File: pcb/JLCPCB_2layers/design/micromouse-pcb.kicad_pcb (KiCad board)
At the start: 2 copper layers, 100 x 120 mm, 135 parts, among them J1 BATT_IN_2S, J10 BATT_IN_XT60 (parallel option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, J5 MOTOR_A_N20_ENCODER, J6 MOTOR_B_N20_ENCODER, J7 USB-C rear (GCT USB4105; VBUS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, Q1 Q_PMOS reverse guard (DMP3098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, Q16 BSS138 (real part; Q_NMOS_GSD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, Q17 BSS138 (real part; Q_NMOS_GSD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, Q18 BSS138 (real part; Q_NMOS_GSD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, Q2 PT334-6B (5mm filtered PT; LO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, Q28 BSS84 (PMOS indicator driver;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, Q29 BSS84 (PMOS indicator driver;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, Q3 PT334-6B (5mm filtered PT; LO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, Q30 BSS84 (PMOS indicator driver;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, Q31 BSS84 (PMOS indicator driver;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, Q32 BSS84 (PMOS indicator driver;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, Q33 BSS84 (PMOS indicator driver;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, Q34 MMBT2222A (buzzer low-side dr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, Q4 PT334-6B (5mm filtered PT; LO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, Q5 PT334-6B (5mm filtered PT; LO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, Q6 PT334-6B (5mm filtered PT; LO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, Q7 PT334-6B (5mm filtered PT; LO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, SW1 BTN_A (start / BOOT), SW2 RESET, SW3 BTN_B, SW4 BTN_C, SW5 PWR ALL (PCM12SMTR slide; sli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, SW6 PWR MOTORS (PCM12SMTR slide; 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, U1 AP63203WU-7 (fixed 3.3V 2A bu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, U2 TB6612FNG, U3 ESP32-S3-WROOM-1-N8R2 (quad P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, U6 USBLC6-2SC6 (SOT-23-6; 2P6 ba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, U7 TPS54302DDCR (6.0V/3A motor b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, U8 BNO055 (9-axis IMU + fusion; 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

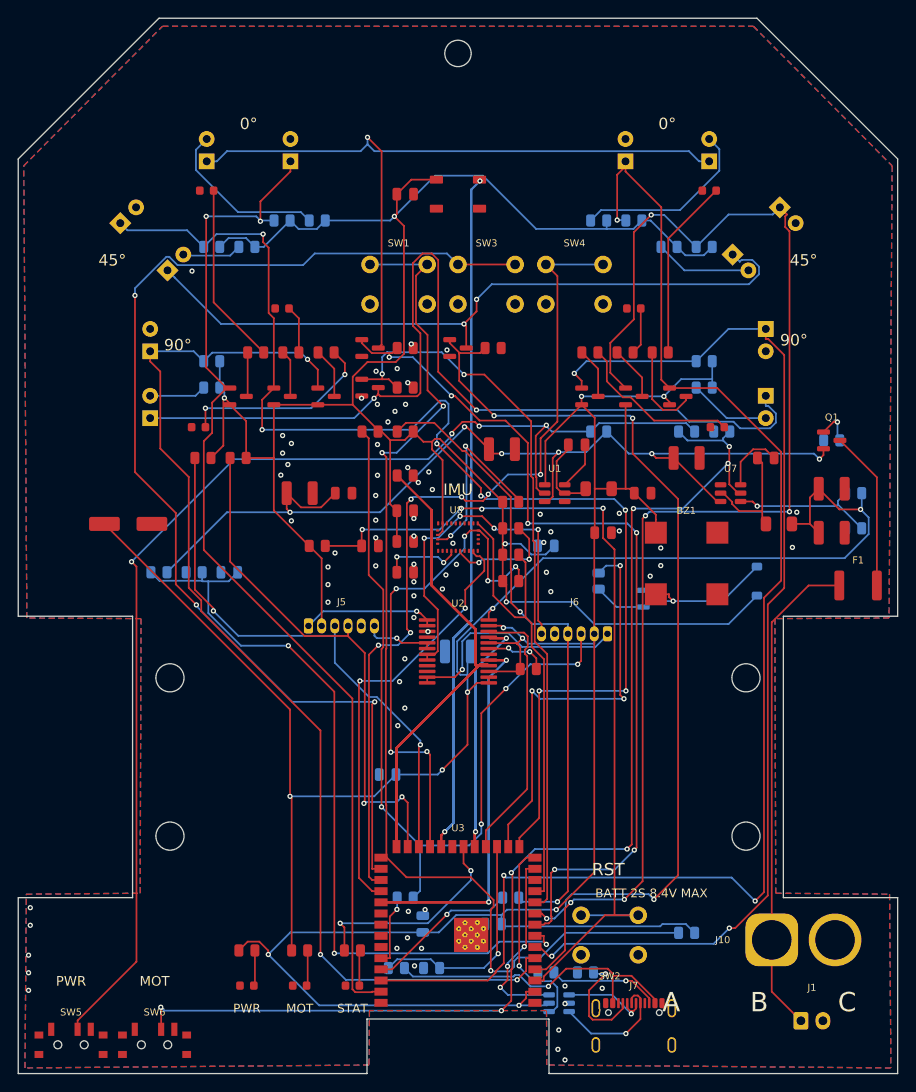
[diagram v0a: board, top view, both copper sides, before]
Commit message: 2-layer PRODUCTION: power-width re-route + full check battery + validated JLC package
Final electronics check (all gates PASS):
- NEW fw/sim_imu.py -- IMU accessibility proven per user request: all 28 BNO055
  pins verified against the official Bosch datasheet Table 5-1 (fetched + read),
  I2C bus electricals (4.7k pull-ups, 199ns rise @400kHz, no contention), and a
  behavioral register-level replay of imu_init()/imu_selftest() (addr 0x28 from
  the COM3 strap, CHIP_ID retry vs 400ms power-on, mode timing vs Table 3-6,
  CLK_SEL kept internal since XIN32/XOUT32 are NC, NDOF fusion up, heading +
  gyro reads). 44/44 PASS.
- AMPACITY FIX: Freerouting had routed every power rail at its 0.2mm default.
  Added tools/dsn_power_class.py (DSN class surgery: power 0.5mm, PLUS3V3
  0.4mm) + tools/route_pipeline.py (motor-bay open + hard-net pre-route +
  inset boundary + DSN export). Re-routed: BATT_RAW/VM_BATT/VM_6V/SW_6V all
  0.5mm, PLUS3V3 0.4mm -> IPC-2152 satisfied with margin. Score 994.73,
  0 signal unrouted.
- sim_flash netlist path fixed (design/ not pcb/); ALL STAGES PASS.
- check_pins 28/28, sim_preflight PASS, impedance PASS, ERC 0.
- DRC 0 errors / 0 parity; GND unconnected floor = 7 non-critical items
  (documented waiver in export_fab: redundant U8 GND pads 2/25 + pour slivers).

JLCPCB compliance + availability:
- Board vs JLC 2-layer limits: min track 0.2 (>=0.127), via 0.6/0.3, clearance
  rule 0.127 -- all within standard capability.
- LCSC map: 44/44 BOM MPNs mapped. BNO055 (C93216) re-verified 2026-07-21:
  LCSC retail down to 2 units -- RESERVE at checkout or pre-source (note
  updated in jlcpcb_lcsc_map.py).

Production package (design/fab_release/jlcpcb/, committed):
- gerbers zip (9 layers, 2-layer set -- export_fab fixed off the 4-layer
  In1/In2 list), Excellon drill with 3.2/3.0 NPTH mounts, BOM + CPL xlsx/csv,
  THT reference.
- NEW tools/validate_jlc_files.py: mechanical JLC-compatibility gate (RS-274X
  headers, aperture >= 0.127mm, outline s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
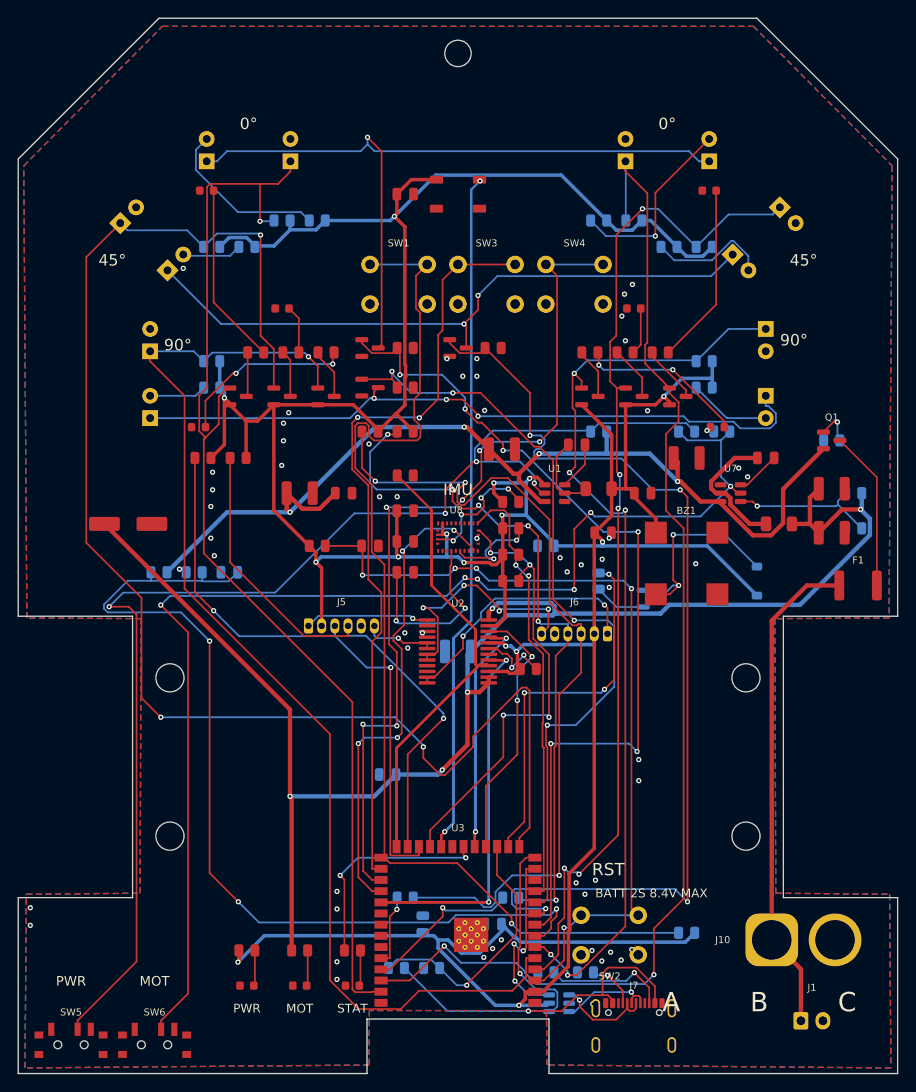
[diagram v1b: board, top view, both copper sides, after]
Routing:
- net BIN2: track 153.2 -> 99.1 mm
- net RGB_DATA: track 200.9 -> 153.2 mm
- net USER_BTN2: track 130.1 -> 87.2 mm, vias 3 -> 2
- net WALL4_SENSE: track 153.0 -> 115.3 mm
- net EMIT_SIDE_K: track 109.4 -> 79.0 mm, vias 2 -> 3
- net PLUS3V3: track 493.1 -> 465.8 mm, vias 11 -> 15
- net WALL3_SENSE: track 143.3 -> 165.8 mm, vias 7 -> 3
- net WALL2_SENSE: track 158.0 -> 139.7 mm, vias 3 -> 2
- net VBAT_SENSE: track 89.9 -> 106.2 mm
- net MOTB_N: track 42.1 -> 27.9 mm
- net WALL6_SENSE: track 121.9 -> 107.7 mm, vias 3 -> 5
- net Net-(U8-CAP): track 9.04 -> 21.5 mm
- net WALL_EMIT_DIAG: track 103.4 -> 114.7 mm
- net WALL1_SENSE: track 116.9 -> 126.6 mm, vias 2 -> 1
- net ESP_EN: track 102.9 -> 93.8 mm, vias 4 -> 5
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
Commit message: 2-layer BOM: stocked JLC parts for the LED + buzzer lines (user assembly review)
From the user's JLCPCB BOM-matching screenshots:

- Indicator LEDs (D23-D28, D30, D31, D33): the multi-line match warning is
  by-design (one red 0603 LED reused across all indicator roles), BUT the
  matched C5875723 has 0 in JLC's assembly pool (LCSC-retail-only). SUB to
  C2286 / KT-0603R -- JLC Basic tier, 3.59M stock (2026-07-21), 0603 pad- and
  Vf-compatible (1.8-2.4V), 300mcd; series resistors unchanged. Also fixed the
  stale "green"/"blue" Value labels at the schematic source: every indicator
  is physically RED (design reuses the wall-indicator part).
- Buzzer BZ1: C3811795 (JLC-consigned listing) hit Inventory shortage. The
  in-stock row is the SAME MPN (CUI CMT-8504-100-SMT-TR) under the regular
  LCSC listing C22359707 (104 stock) -- exact drop-in, verified not a
  substitute. BOM now carries C22359707.

Propagated: schematic + netlist regenerated, ERC 0, check_pins 28/28,
sim_imu PASS, sync_board_meta (2 values), DRC 0 errors / 0 parity,
export_fab ALL GATES, JLC package re-exported + validate_jlc_files ALL PASS.
Board copper untouched (diff = 2 value strings).

Co-Authored-By: Claude Fable 5 <noreply@anthropic.com>
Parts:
- D30: value Power LED 0603 green (JLC good-stock) -> Power LED 0603 red (JLC good-stock)
- D31: value Status LED 0603 blue (JLC good-stock) -> Status LED 0603 red (JLC good-stock)
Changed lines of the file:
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@@
 			)
 		)
-		(property "Value" "Status LED 0603 blue (JLC good-stock)"
+		(property "Value" "Status LED 0603 red (JLC good-stock)"
 			(at 0 1.43 0)
 			(layer "F.Fab")
@@
 			)
 		)
-		(property "Value" "Power LED 0603 green (JLC good-stock)"
+		(property "Value" "Power LED 0603 red (JLC good-stock)"
 			(at 0 1.43 0)
 			(layer "F.Fab")

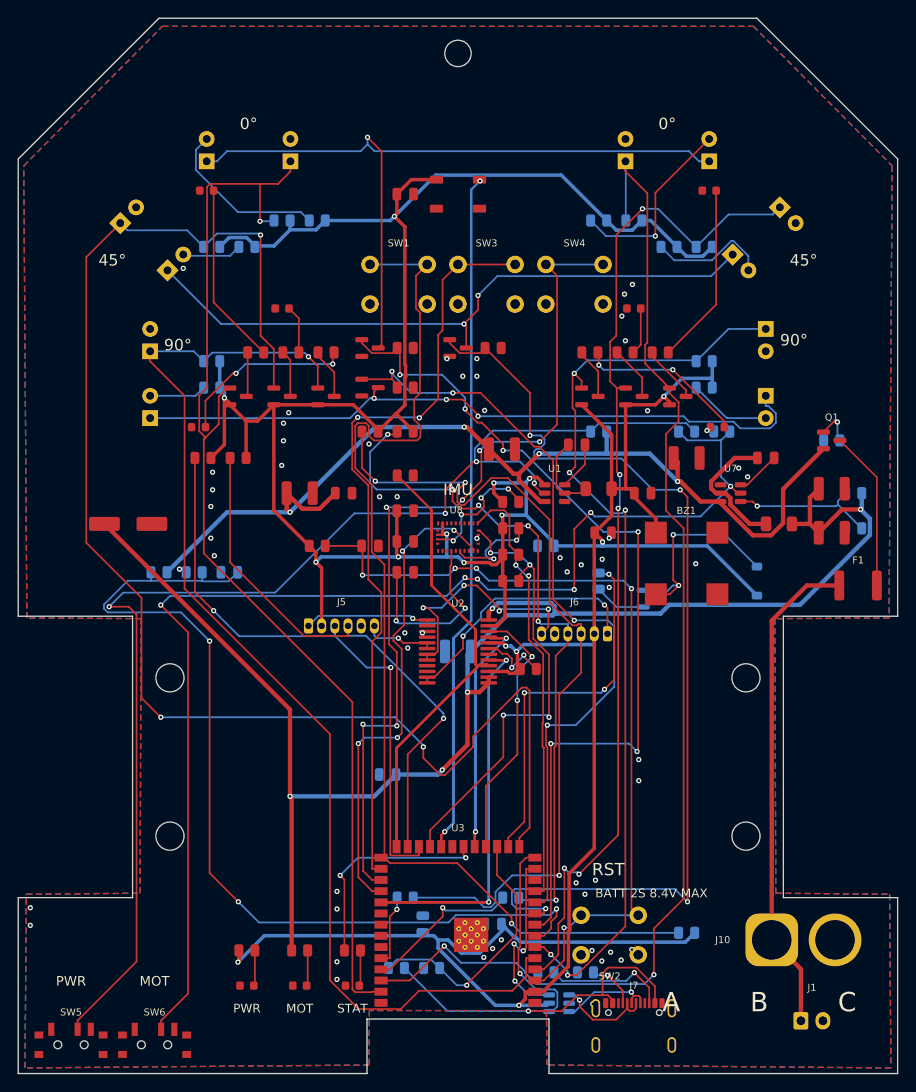
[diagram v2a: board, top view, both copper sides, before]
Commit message: 2-layer PRODUCTION: final JLCPCB + Lion Circuits release (wall sensors only)
Production-ready release for the 2-layer micromouse board (wall sensors
only, no line array/mux/JTAG): U8 (IMU) + U2 (motor driver) flipped to
the bottom layer, full clean-slate Freerouting re-route, GND pour
fragment bridging, BOM duplicate-part merge, and DRC cleanup (0 errors,
0 warnings). Includes matching production folders for both JLCPCB and
Lion Circuits (BOM, CPL, gerbers).

Co-Authored-By: Claude Sonnet 5 <noreply@anthropic.com>
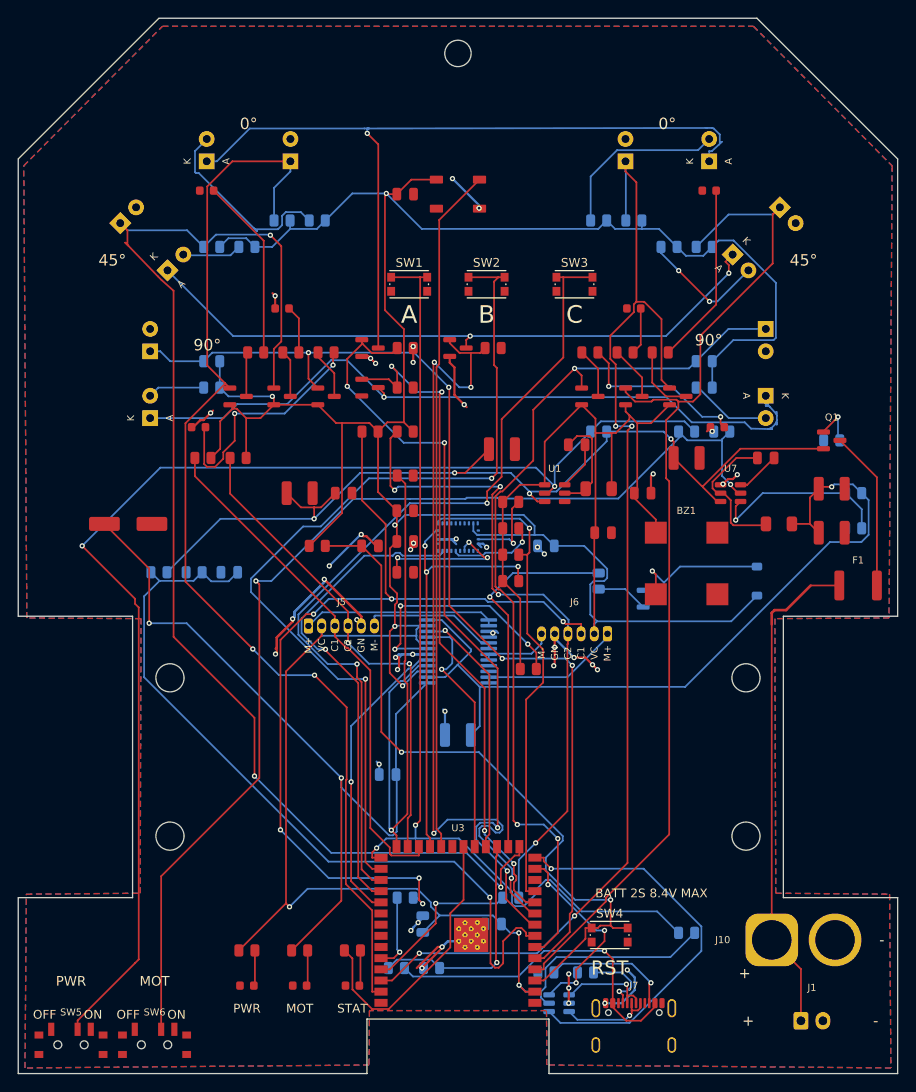
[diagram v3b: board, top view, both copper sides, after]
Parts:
- SW1: footprint Button_Switch_THT:SW_PUSH_6mm -> Button_Switch_SMD:SW_Push_1P1T_NO_CK_KMR2
- SW2: value RESET -> BTN_B; footprint Button_Switch_THT:SW_PUSH_6mm -> Button_Switch_SMD:SW_Push_1P1T_NO_CK_KMR2
- SW3: value BTN_B -> BTN_C; footprint Button_Switch_THT:SW_PUSH_6mm -> Button_Switch_SMD:SW_Push_1P1T_NO_CK_KMR2
- SW4: value BTN_C -> RESET; footprint Button_Switch_THT:SW_PUSH_6mm -> Button_Switch_SMD:SW_Push_1P1T_NO_CK_KMR2
- U2, U8: moved to B.Cu
- moved SW4 76.6 mm to (67.2, 104.2)
- moved SW2 72.6 mm to (53.2, 30.2)
- moved SW3 13.4 mm to (63.2, 30.2)
- moved C11 9.50 mm to (50.0, 81.5)
- moved SW1 4.99 mm to (44.5, 30.2)
- turned U2 to 180 degrees
- turned U8 to 180 degrees
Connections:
- SW2 pad 1: ESP_EN -> USER_BTN2
- SW3 pad 1: USER_BTN2 -> USER_BTN3
- SW4 pad 1: USER_BTN3 -> ESP_EN
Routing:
- net GND: track 0.00 -> 127.1 mm, vias 58 -> 45
- net RGB_DATA: track 153.2 -> 78.1 mm, vias 2 -> 0
- net BIN1: track 82.3 -> 33.8 mm, vias 2 -> 1
- net PLUS3V3: track 465.8 -> 508.3 mm, vias 15 -> 8
- net BIN2: track 99.1 -> 65.1 mm, vias 0 -> 1
- net USB_DP: track 22.5 -> 46.4 mm
- net WALL_EMIT_DIAG: track 114.7 -> 93.0 mm
- net AIN1: track 49.2 -> 28.9 mm, vias 2 -> 1
- net Net-(U2-STBY): track 8.30 -> 28.4 mm, vias 2 -> 3
- net WALL3_SENSE: track 165.8 -> 146.0 mm
- net MOTB_N: track 27.9 -> 8.27 mm, vias 4 -> 0
- net VBAT_SENSE: track 106.2 -> 89.6 mm, vias 3 -> 1
- net MOT_EN: track 140.5 -> 124.9 mm, vias 6 -> 2
- net USER_BTN2: track 87.2 -> 101.2 mm
- net WALL_EMIT_FRONT: track 101.2 -> 87.8 mm, vias 6 -> 4
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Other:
- board text added: "+"
- board text added: "-"
- board text added: "C1"
- board text added: "C2"
- board text added: "GN"
- board text added: "K"
- board text added: "M+"
- board text added: "M-"
- board text added: "OFF"
- board text added: "ON"
- board text added: "VC"
